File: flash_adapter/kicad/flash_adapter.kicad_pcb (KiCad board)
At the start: 2 copper layers, 48.4 x 43.6 mm, 6 parts, among them J1 Conn_01x10, J3 DS1044-160G

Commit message: Updated flash adapter
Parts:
- added J2: Conn_01x10, Connector_PinSocket_2.54mm:PinSocket_1x10_P2.54mm_Vertical, F.Cu at (126.7, 93.2)
- added R2: 10k, Resistor_SMD:R_0805_2012Metric, F.Cu at (157.0, 89.5)
- added R3: 10k, Resistor_SMD:R_0805_2012Metric, F.Cu at (157.0, 91.9)
- added REF**: OSHW-Logo2_7.3x6mm_SilkScreen, Symbol:OSHW-Logo2_7.3x6mm_SilkScreen, F.Cu at (125.9, 87.8)
- moved R1 44.9 mm to (134.4, 87.2)
- moved D1 40.7 mm to (134.4, 89.7)
- moved C1 23.3 mm to (157.0, 94.3)
- moved J3 4.31 mm to (147.1, 106.3)
- moved REF** 4.10 mm to (130.2, 124.0)
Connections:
- C1 pad 1: unconnected-(C1-Pad1) -> VIO_{DOCK}
- C1 pad 2: unconnected-(C1-Pad2) -> GND
- J1 pad 2: RST -> Net-(J1-Pin_2)
- J1 pad 3: BOOT -> Net-(J1-Pin_3)
- J1 pad 4: UART_TX -> HOLD
- J1 pad 5: UART_RX -> WP
- J1 pad 6: IO6 -> MOSI
- J1 pad 7: IO8 -> CS
- J1 pad 8: IO9 -> SCLK
- J1 pad 9: IO10 -> MISO
- J3 pad 1: unconnected-(J3-Pad1) -> CS
- J3 pad 10: unconnected-(J3-Pad10) -> SCLK
- J3 pad 11: unconnected-(J3-Pad11) -> HOLD
- J3 pad 12: unconnected-(J3-Pad12) -> VIO_{DOCK}
- J3 pad 13: unconnected-(J3-Pad13) -> MISO
- J3 pad 14: unconnected-(J3-Pad14) -> SCLK
- J3 pad 15: unconnected-(J3-Pad15) -> HOLD
- J3 pad 16: unconnected-(J3-Pad16) -> VIO_{DOCK}
- J3 pad 2: unconnected-(J3-Pad2) -> MOSI
- J3 pad 3: unconnected-(J3-Pad3) -> WP
- J3 pad 4: unconnected-(J3-Pad4) -> GND
- J3 pad 5: unconnected-(J3-Pad5) -> CS
- J3 pad 6: unconnected-(J3-Pad6) -> MOSI
- J3 pad 7: unconnected-(J3-Pad7) -> WP
- J3 pad 8: unconnected-(J3-Pad8) -> GND
- J3 pad 9: unconnected-(J3-Pad9) -> MISO
- R1 pad 1: VOUT -> VIO_{DOCK}
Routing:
- net VIO_{DOCK}: track 0.00 -> 64.2 mm
- net CS: track 0.00 -> 33.8 mm
- net SCLK: track 0.00 -> 28.8 mm
- net HOLD: track 0.00 -> 28.8 mm
- net WP: track 0.00 -> 20.9 mm
- net Net-(J1-Pin_2): track 0.00 -> 3.91 mm
- net MOSI: track 0.00 -> 3.91 mm
- net MISO: track 0.00 -> 3.91 mm
- net Net-(J1-Pin_3): track 0.00 -> 3.91 mm
- net Net-(D1-A): track 0.00 -> 2.51 mm
- net GND: track 0.00 -> 1.52 mm, vias 0 -> 1
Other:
- board size 48.4 x 43.6 mm -> 41.2 x 43.5 mm
- board text added: "1"
- board text added: "5"
- board text added: "DIP8"
- board text added: "GND MISO SCLK CS MOSI U0RX U0TX BOOT RST VIO"
- board text removed: "GND IO10 IO9 IO8 IO6 U0RX U0TX BOOT RST VIO"
- board text removed: "ISOLATED/COUPLED"
- board text removed: "THT Flash"

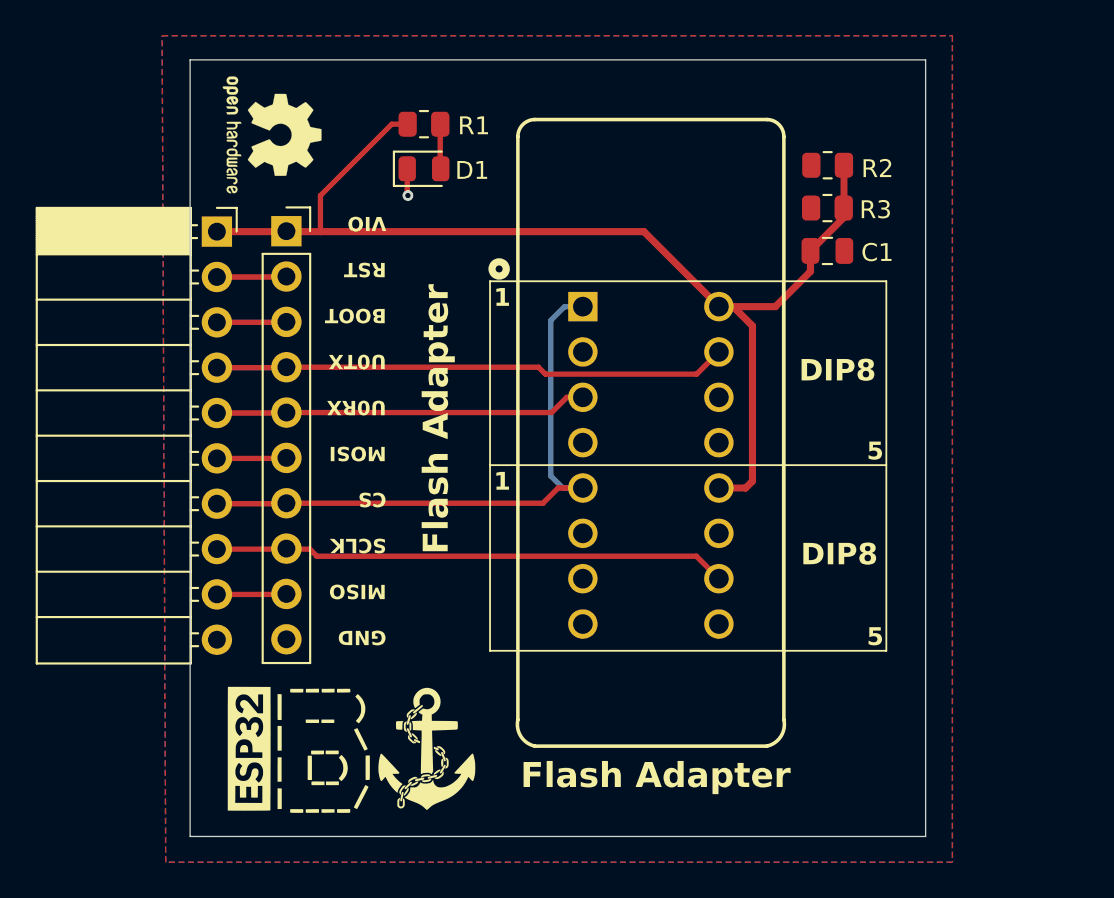
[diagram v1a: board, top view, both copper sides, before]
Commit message: Added separate CS#
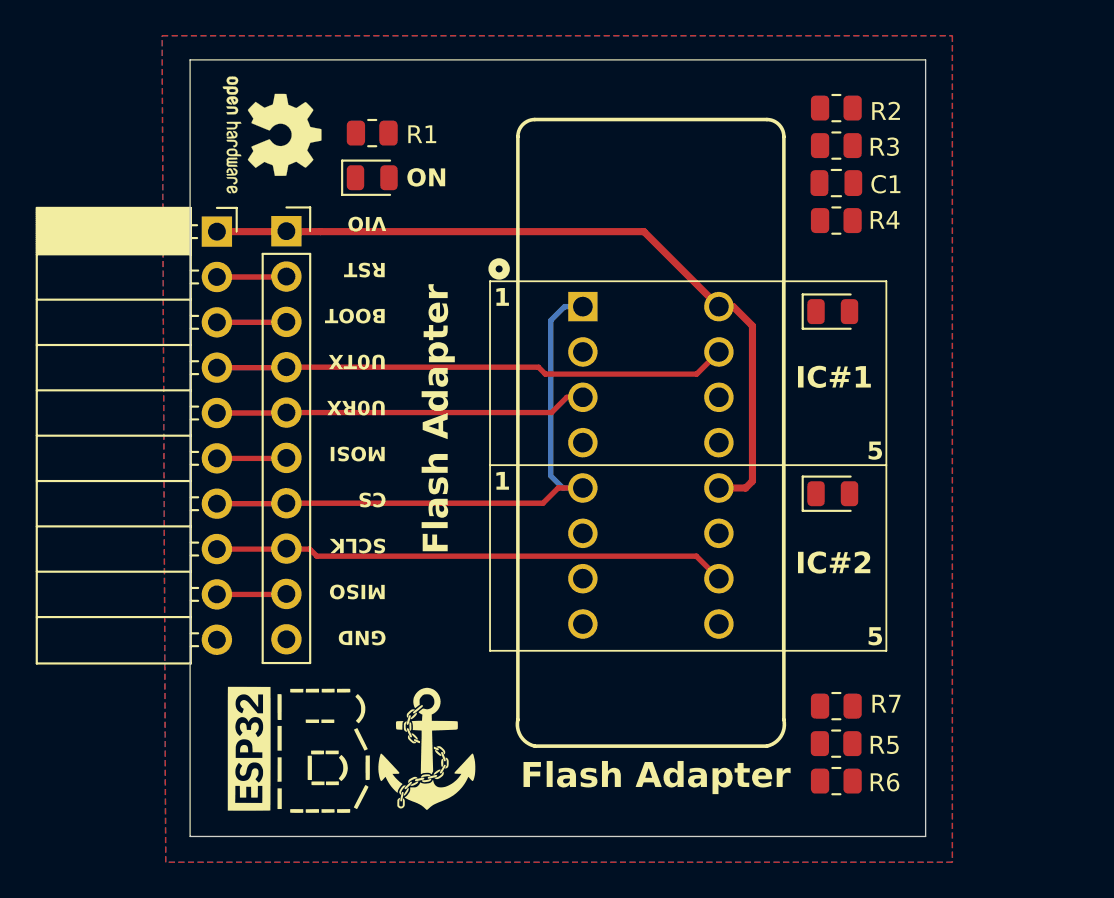
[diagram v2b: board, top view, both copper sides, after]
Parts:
- added D2: GREEN, LED_SMD:LED_0805_2012Metric, F.Cu at (157.3, 97.7)
- added D3: GREEN, LED_SMD:LED_0805_2012Metric, F.Cu at (157.3, 107.9)
- added R4: 1k, Resistor_SMD:R_0805_2012Metric, F.Cu at (157.5, 92.6)
- added R5: 10k, Resistor_SMD:R_0805_2012Metric, F.Cu at (157.5, 121.9)
- added R6: 10k, Resistor_SMD:R_0805_2012Metric, F.Cu at (157.5, 124.0)
- added R7: 1k, Resistor_SMD:R_0805_2012Metric, F.Cu at (157.5, 119.8)
- moved C1 3.83 mm to (157.5, 90.5)
- moved R3 3.54 mm to (157.5, 88.4)
- moved R2 3.24 mm to (157.5, 86.3)
- moved D1 2.94 mm to (131.5, 90.2)
- moved R1 2.94 mm to (131.5, 87.7)
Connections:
- J1 pad 3: Net-(J1-Pin_3) -> CS#2
- J1 pad 7: CS -> CS#1
- J2 pad 3: Net-(J1-Pin_3) -> CS#2
- J2 pad 7: CS -> CS#1
- J3 pad 1: CS -> CS#1
- J3 pad 5: CS -> CS#2
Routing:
- net CS: track 33.8 -> 0.00 mm
- net (no net): track 0.00 -> 33.8 mm
- net VIO_{DOCK}: track 64.2 -> 42.9 mm
- net Net-(J1-Pin_3): track 3.91 -> 0.00 mm
- net CS#2: track 0.00 -> 3.91 mm
- net Net-(D1-A): track 2.51 -> 0.00 mm
- net GND: track 1.52 -> 0.00 mm, vias 1 -> 0
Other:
- board text added: "IC#1"
- board text added: "IC#2"
- board text added: "ON"
- board text removed: "DIP8"

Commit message: Finished routing
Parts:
- added D4: BLUE, LED_SMD:LED_0805_2012Metric, F.Cu at (130.8, 88.0)
- added R8: 1k, Resistor_SMD:R_0805_2012Metric, F.Cu at (134.4, 85.7)
- moved R1 2.12 mm to (130.8, 85.7)
- moved R5 2.10 mm to (157.5, 124.0)
- moved R6 2.10 mm to (157.5, 121.9)
- moved D1 0.70 mm to (130.8, 90.2)
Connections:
- net Net-(J1-Pin_2) renamed IO13
- J1 pad 3: CS#2 -> CS#1
- J1 pad 7: CS#1 -> CS#2
- J2 pad 3: CS#2 -> CS#1
- J2 pad 7: CS#1 -> CS#2
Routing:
- net CS#1: track 0.00 -> 70.7 mm, vias 0 -> 2
- net CS#2: track 3.91 -> 51.6 mm, vias 0 -> 2
- net VIO_{DOCK}: track 42.9 -> 86.9 mm, vias 0 -> 1
- net WP: track 20.9 -> 62.3 mm, vias 0 -> 3
- net MISO: track 3.91 -> 38.7 mm, vias 0 -> 1
- net (no net): track 33.8 -> 0.00 mm
- net MOSI: track 3.91 -> 31.7 mm, vias 0 -> 2
- net HOLD: track 28.8 -> 56.1 mm, vias 0 -> 2
- net IO13: track 3.91 -> 19.2 mm, vias 0 -> 1
- net Net-(D3-A): track 0.00 -> 15.2 mm
- net SCLK: track 28.8 -> 39.1 mm, vias 0 -> 1
- net Net-(D2-A): track 0.00 -> 5.17 mm
- net Net-(D1-A): track 0.00 -> 4.94 mm
- net Net-(D4-A): track 0.00 -> 4.67 mm
- net GND: track 0.00 -> 3.65 mm, vias 0 -> 9
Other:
- board text added: "IO13"
